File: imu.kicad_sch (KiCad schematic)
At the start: 9 parts, among them U5 MPU-6500

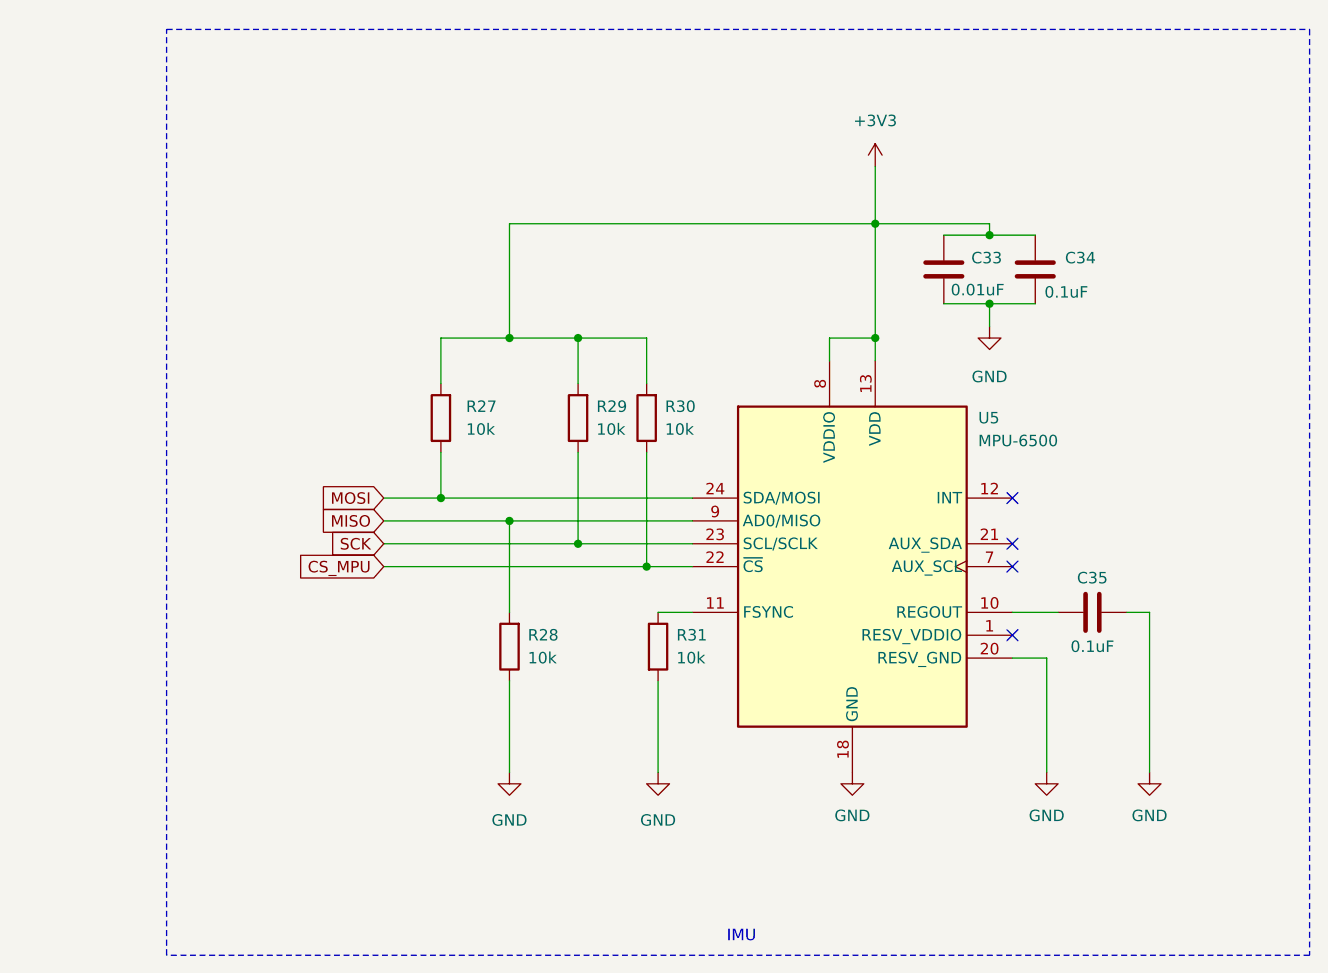
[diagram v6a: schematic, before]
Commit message: Fixed short cirquit, minors
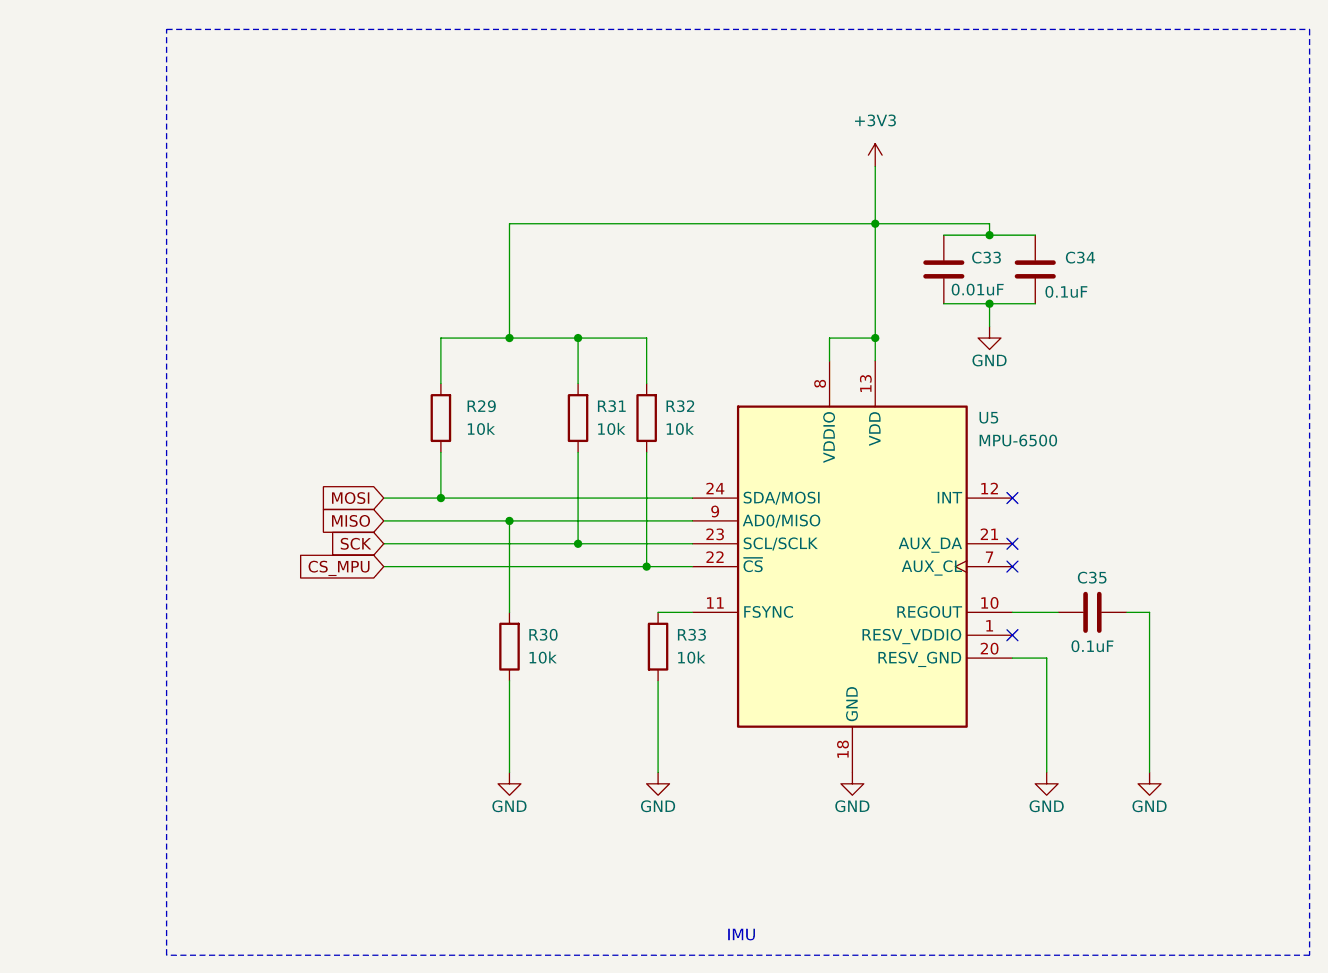
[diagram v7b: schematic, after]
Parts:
- renumbered R27 to R29, R28 to R30, R29 to R31, R30 to R32, R31 to R33

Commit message: Add drivers, stepdown on VIPER115, fixes
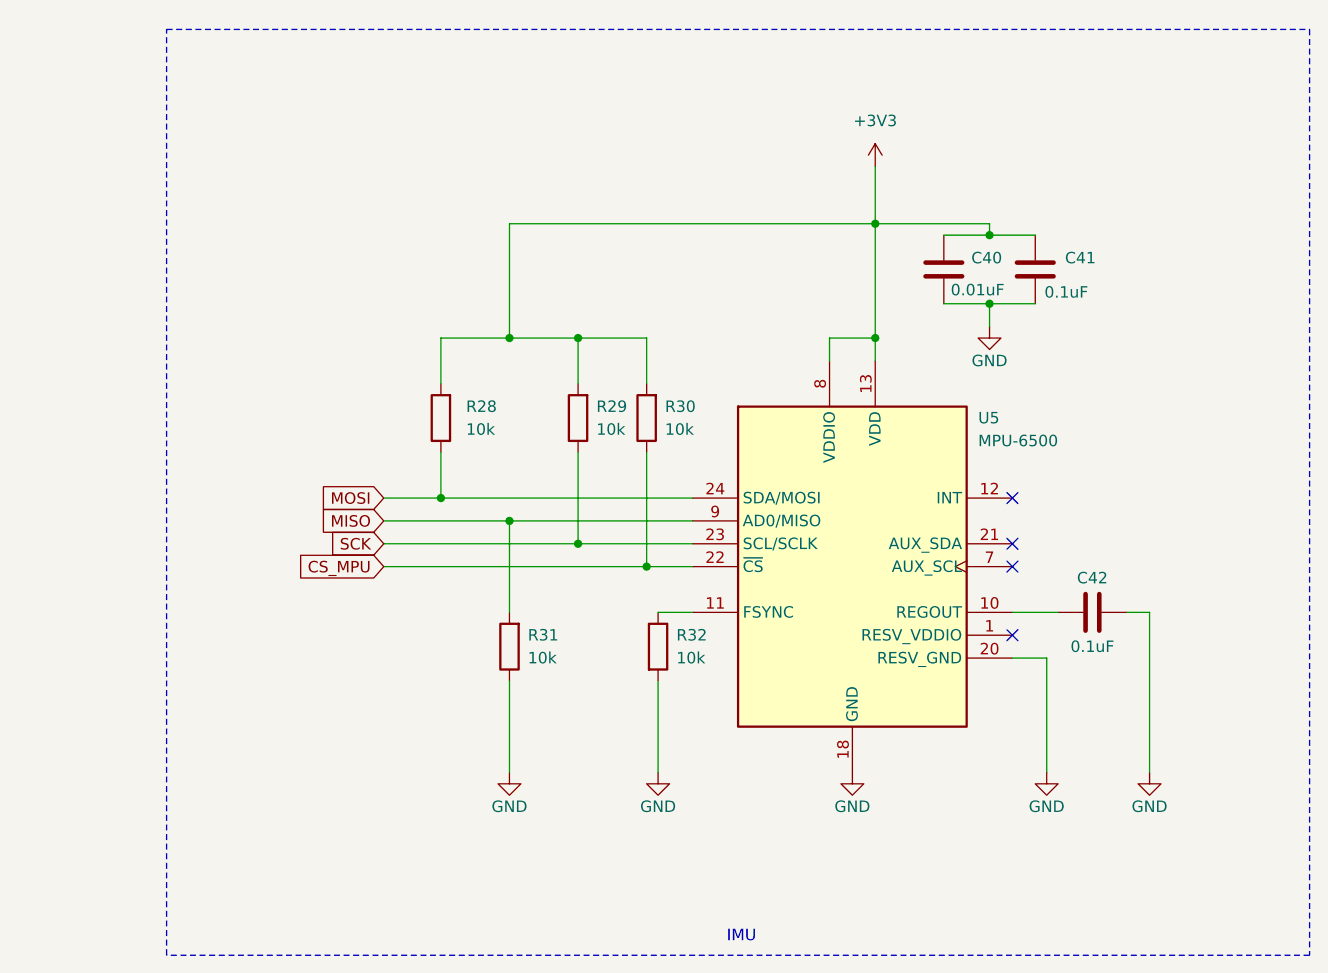
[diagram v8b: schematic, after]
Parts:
- renumbered C33 to C40, C34 to C41, C35 to C42, R29 to R28, R31 to R29, R32 to R30, R30 to R31, R33 to R32
